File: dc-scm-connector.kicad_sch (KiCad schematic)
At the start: 85 parts, among them J3 PCB-Edge_DC-SCM-2.1_2x84_Rev-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

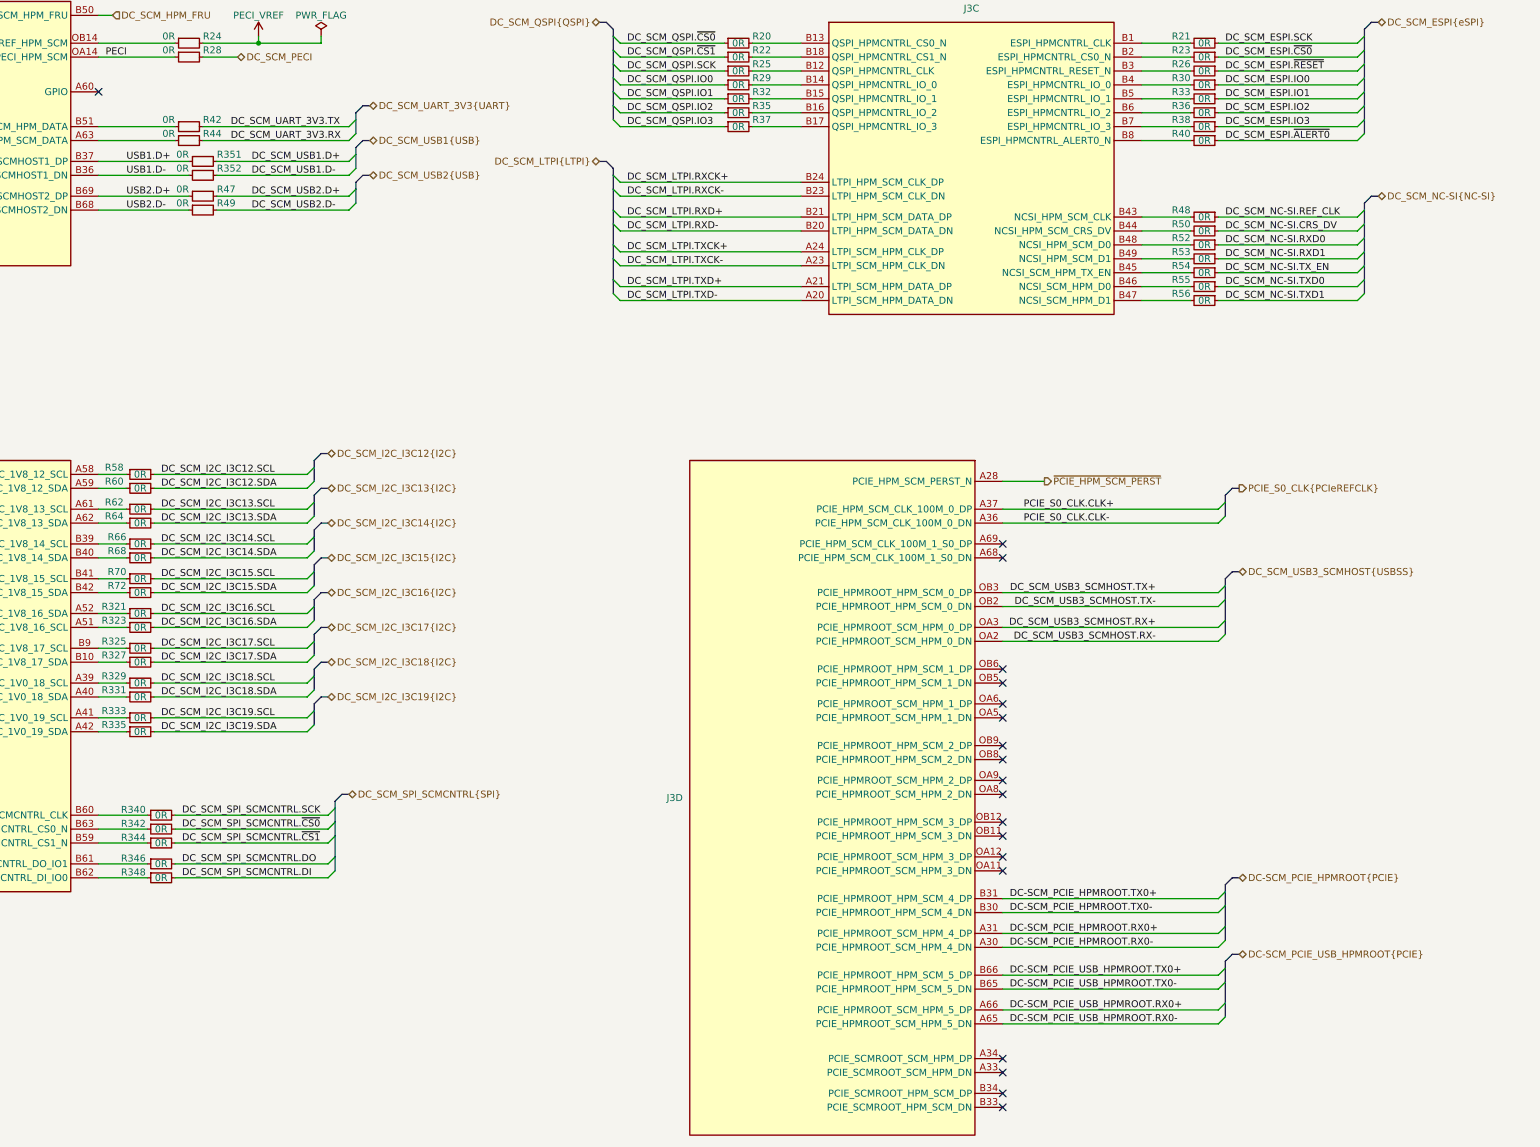
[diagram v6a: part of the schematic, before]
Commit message: [#100595] Update connections according to client request
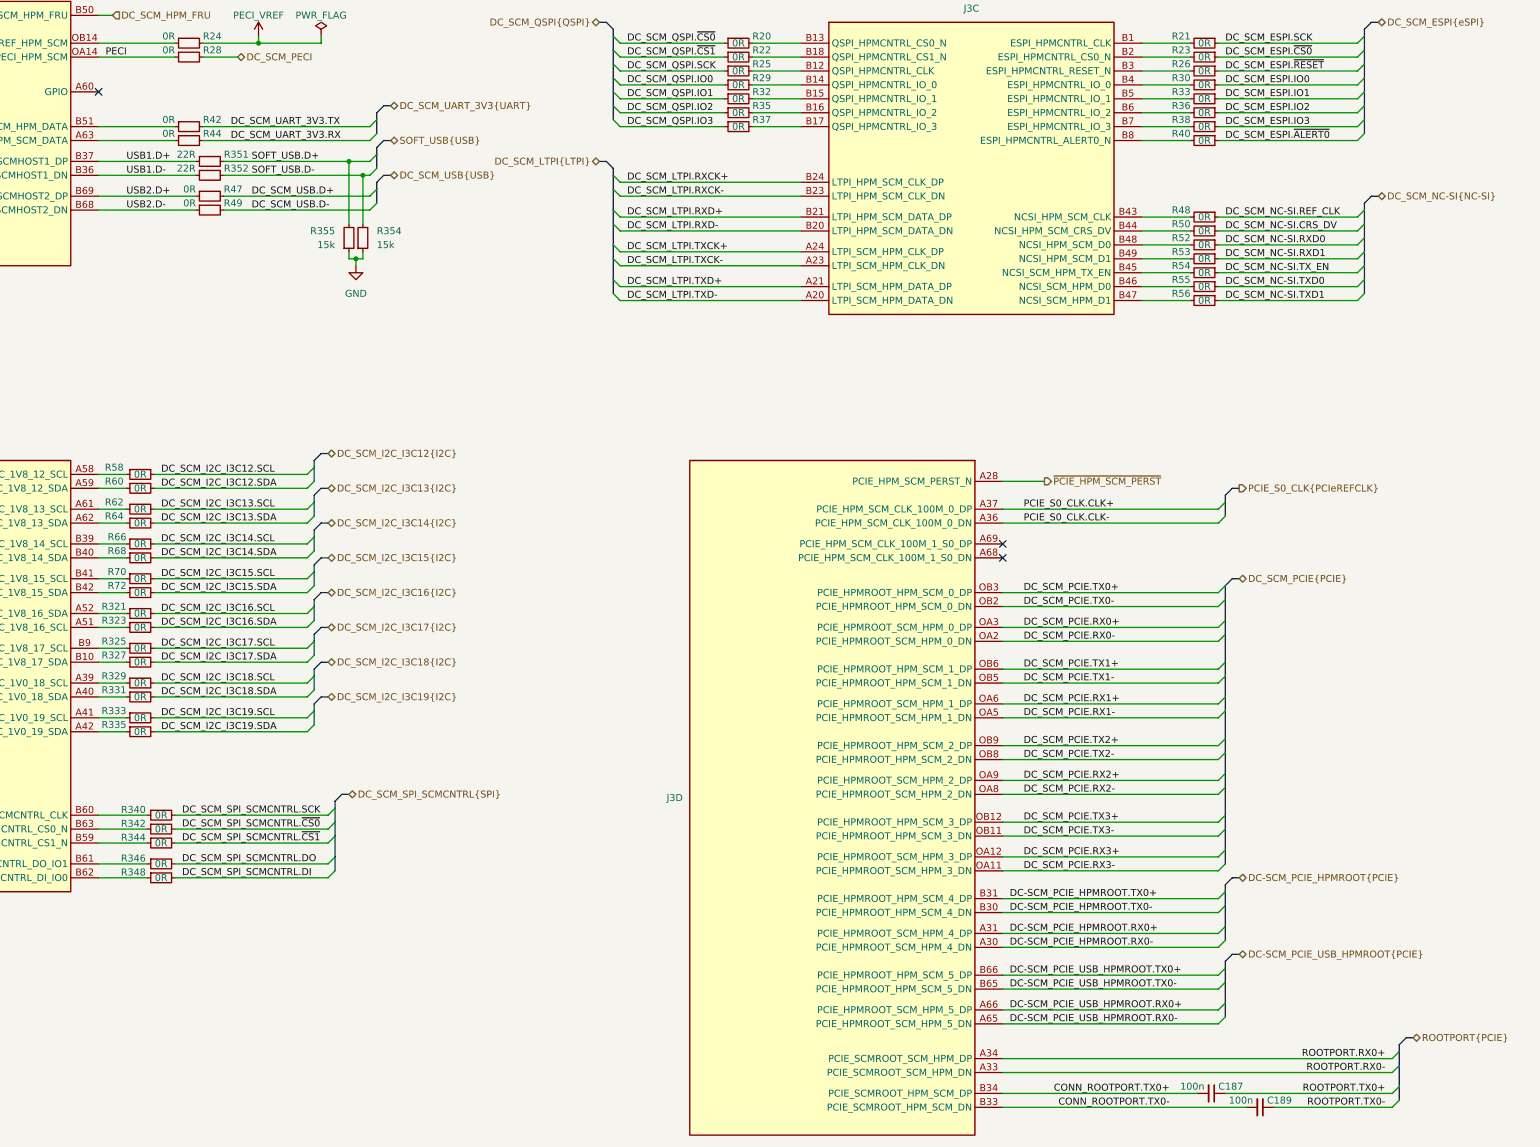
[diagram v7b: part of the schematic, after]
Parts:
- removed R351, R352: R_0R_0402, antmicro-footprints:R_0402_1005Metric, symbol antmicroResistors0402:R_0R_0402
- added C187, C189: C_100n_0402, antmicro-footprints:C_0402_1005Metric, symbol antmicroCapacitors0402:C_100n_0402
- added R351, R352: R_22R_0402, antmicro-footprints:R_0402_1005Metric, symbol antmicroResistors0402:R_22R_0402
- added R354, R355: R_15k_0402, antmicro-footprints:R_0402_1005Metric, symbol antmicroResistors0402:R_15k_0402
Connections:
- net GND: now also R354.1, R355.1
- net USB1.D+: now also R351.1
- net USB1.D-: now also R352.1
- net ROOTPORT.RX0-: now reaches J3.A33 (PCIE_SCMROOT_SCM_HPM_DN)
- net ROOTPORT.RX0+: now reaches J3.A34 (PCIE_SCMROOT_SCM_HPM_DP)
- net CONN_ROOTPORT.TX0-: now reaches J3.B33 (PCIE_SCMROOT_HPM_SCM_DN)
- net CONN_ROOTPORT.TX0-: now also C189.2
- net CONN_ROOTPORT.TX0+: now reaches J3.B34 (PCIE_SCMROOT_HPM_SCM_DP)
- net CONN_ROOTPORT.TX0+: now also C187.2
- net DC_SCM_PCIE.RX3-: now reaches J3.OA11 (PCIE_HPMROOT_SCM_HPM_3_DN)
- net DC_SCM_PCIE.RX3+: now reaches J3.OA12 (PCIE_HPMROOT_SCM_HPM_3_DP)
- net DC_SCM_PCIE.RX1-: now reaches J3.OA5 (PCIE_HPMROOT_SCM_HPM_1_DN)
- net DC_SCM_PCIE.RX1+: now reaches J3.OA6 (PCIE_HPMROOT_SCM_HPM_1_DP)
- net DC_SCM_PCIE.RX2-: now reaches J3.OA8 (PCIE_HPMROOT_SCM_HPM_2_DN)
- net DC_SCM_PCIE.RX2+: now reaches J3.OA9 (PCIE_HPMROOT_SCM_HPM_2_DP)
- net DC_SCM_PCIE.TX3-: now reaches J3.OB11 (PCIE_HPMROOT_HPM_SCM_3_DN)
- net DC_SCM_PCIE.TX3+: now reaches J3.OB12 (PCIE_HPMROOT_HPM_SCM_3_DP)
- net DC_SCM_PCIE.TX1-: now reaches J3.OB5 (PCIE_HPMROOT_HPM_SCM_1_DN)
- net DC_SCM_PCIE.TX1+: now reaches J3.OB6 (PCIE_HPMROOT_HPM_SCM_1_DP)
- net DC_SCM_PCIE.TX2-: now reaches J3.OB8 (PCIE_HPMROOT_HPM_SCM_2_DN)
- net DC_SCM_PCIE.TX2+: now reaches J3.OB9 (PCIE_HPMROOT_HPM_SCM_2_DP)
- net DC_SCM_USB2.D+ renamed DC_SCM_USB.D+
- net DC_SCM_USB2.D- renamed DC_SCM_USB.D-
- net DC_SCM_USB3_SCMHOST.RX+ renamed DC_SCM_PCIE.RX0+
- net DC_SCM_USB3_SCMHOST.RX- renamed DC_SCM_PCIE.RX0-
- net DC_SCM_USB3_SCMHOST.TX+ renamed DC_SCM_PCIE.TX0+
- net DC_SCM_USB3_SCMHOST.TX- renamed DC_SCM_PCIE.TX0-
- new net ROOTPORT.TX0+: C187.1
- new net ROOTPORT.TX0-: C189.1
- new net SOFT_USB.D+: R351.2, R355.2
- new net SOFT_USB.D-: R352.2, R354.2
- no-connect marks 19 -> 3
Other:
- moved on the sheet: R47, R49

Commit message: [#100501] Fix DC-SCM I2C_16 SDA/SCL swap
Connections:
- net at J3.A51 (I2C_I3C_1V8_16_SCL): now also R321.1; no longer R323.1
- net at J3.A52 (I2C_I3C_1V8_16_SDA): now also R323.1; no longer R321.1
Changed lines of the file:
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@@
 			(justify left bottom)
 		)
-		(property "Netclass" "50Ohm-se"
+		(property "Net Class" "50Ohm-se"
 			(at 44.45 191.77 0)
 			(show_name no)
@@
 			(justify right bottom)
 		)
-		(property "Netclass" "50Ohm-se"
+		(property "Net Class" "50Ohm-se"
 			(at 383.54 48.26 0)
 			(show_name no)
@@
 			(justify right bottom)
 		)
-		(property "Netclass" "85Ohm-diff"
+		(property "Net Class" "85Ohm-diff"
 			(at 358.14 204.47 0)
 			(show_name no)
@@
 			(justify right bottom)
 		)
-		(property "Netclass" "85Ohm-diff"
+		(property "Net Class" "85Ohm-diff"
 			(at 319.4685 247.65 0)
 			(show_name no)
@@
 			(justify right bottom)
 		)
-		(property "Netclass" "90Ohm-diff"
+		(property "Net Class" "90Ohm-diff"
 			(at 150.622 82.55 0)
 			(show_name no)
@@
 			(justify right bottom)
 		)
-		(property "Netclass" "85Ohm-diff"
+		(property "Net Class" "85Ohm-diff"
 			(at 358.14 218.44 0)
 			(show_name no)
@@
 			(justify left bottom)
 		)
-		(property "Netclass" "50Ohm-se"
+		(property "Net Class" "50Ohm-se"
 			(at 274.828 43.18 0)
 			(show_name no)
@@
 			(justify right bottom)
 		)
-		(property "Netclass" "50Ohm-se"
+		(property "Net Class" "50Ohm-se"
 			(at 195.58 189.23 0)
 			(show_name no)
@@
 			(justify right bottom)
 		)
-		(property "Netclass" "90Ohm-diff"
+		(property "Net Class" "90Ohm-diff"
 			(at 203.2 69.85 0)
 			(show_name no)
@@
 			(justify left bottom)
 		)
-		(property "Netclass" "50Ohm-se"
+		(property "Net Class" "50Ohm-se"
 			(at 238.76 48.26 0)
 			(show_name no)
@@
 			(justify right bottom)
 		)
-		(property "Netclass" "90Ohm-diff"
+		(property "Net Class" "90Ohm-diff"
 			(at 203.2 76.2 0)
 			(show_name no)
@@
 			(justify left bottom)
 		)
-		(property "Netclass" "100Ohm-diff"
+		(property "Net Class" "100Ohm-diff"
 			(at 239.268 73.66 0)
 			(show_name no)
@@
 			(justify left bottom)
 		)
-		(property "Netclass" "50Ohm-se"
+		(property "Net Class" "50Ohm-se"
 			(at 341.122 43.18 0)
 			(show_name no)
@@
 			(justify right bottom)
 		)
-		(property "Netclass" "50Ohm-se"
+		(property "Net Class" "50Ohm-se"
 			(at 84.5185 205.74 0)
 			(show_name no)
@@
 			(justify right bottom)
 		)
-		(property "Netclass" "85Ohm-diff"
+		(property "Net Class" "85Ohm-diff"
 			(at 389.636 233.68 0)
 			(show_name no)
@@
 			(justify right bottom)
 		)
-		(property "Netclass" "50Ohm-se"
+		(property "Net Class" "50Ohm-se"
 			(at 149.2885 204.47 0)
 			(show_name no)
@@
 	)
 	(symbol
+		(lib_name "PCB-Edge_DC-SCM-2.1_2x84_Rev-1-1_1")
 		(lib_id "antmicroEdgeConnectors:PCB-Edge_DC-SCM-2.1_2x84_Rev-1-1")
 		(at 86.36 127 0)
